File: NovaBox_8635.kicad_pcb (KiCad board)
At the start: 2 copper layers, 53 parts, among them P1 MH, P2 MH, P3 MH, P4 MH, Q1 MMBT3904_l, Q2 IRLML6344, SW1 NEXT, SW2 PREV, SW3 PP, SW4 VOL+, SW5 VOL-, SW6 ON/OFF, U1 CSR8635_MODULE, U2 CSR_DebugSmall, U3 PAM8304, U4 PAM8304

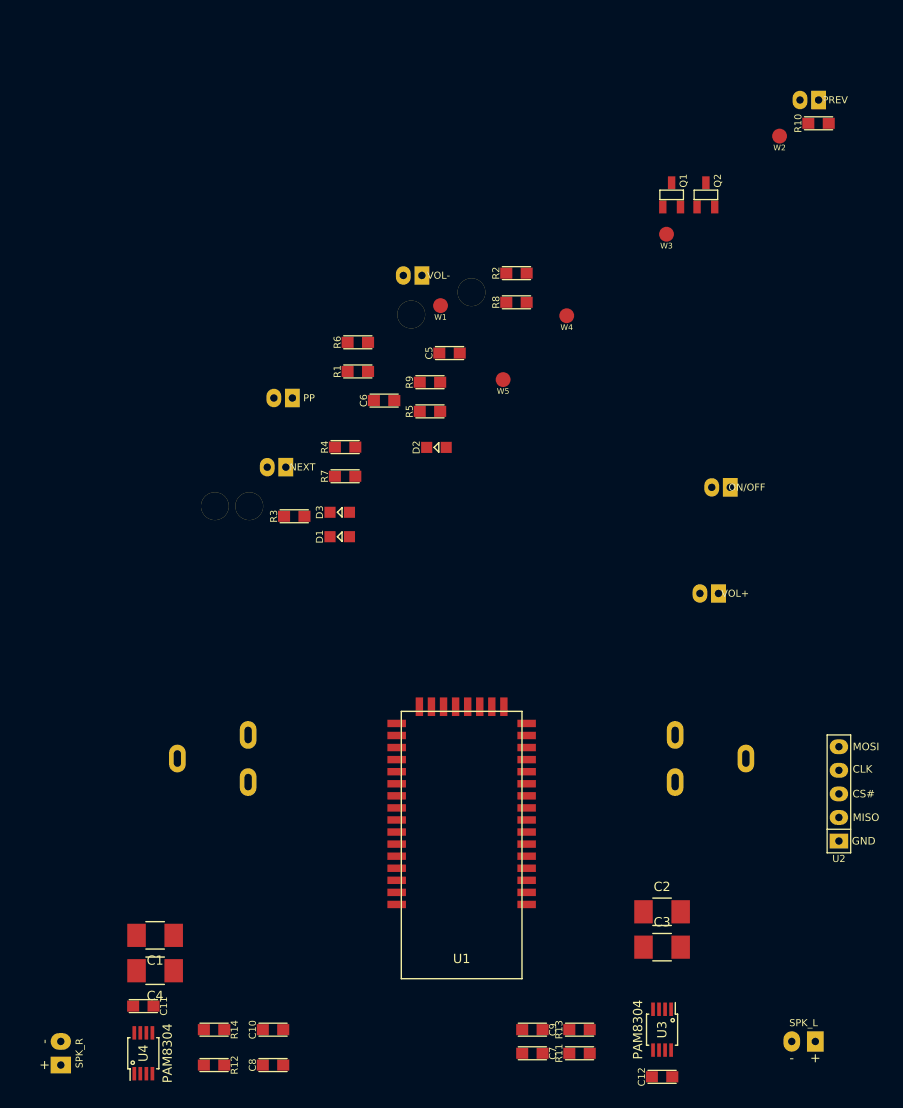
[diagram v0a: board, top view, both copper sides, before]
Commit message: CSR8635 pcb layout
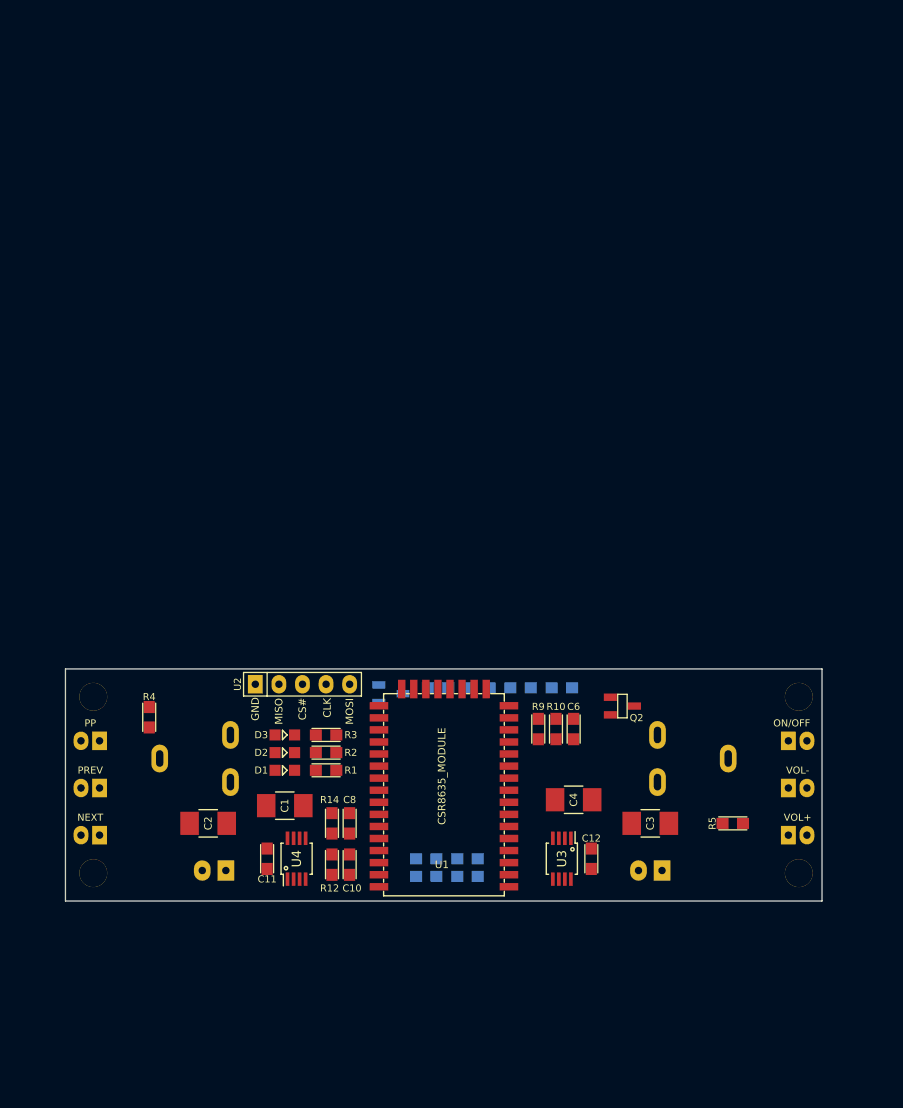
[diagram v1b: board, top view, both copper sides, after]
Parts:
- removed W1: P16, NovaBox:TestPad
- removed W2: P9, NovaBox:TestPad
- removed W3: P0, NovaBox:TestPad
- removed W4: P1, NovaBox:TestPad
- removed W5: P8, NovaBox:TestPad
- C5, C7, C9, Q1, R11, R13, R6, R7, R8, S1, S2: moved to B.Cu
- moved SW2 107.2 mm to (66.7, 123.8)
- moved P4 74.3 mm to (143.0, 133.0)
- moved R10 71.1 mm to (116.8, 117.5), turned to 90 degrees
- moved P2 69.2 mm to (67.0, 133.0)
- moved SW5 69.1 mm to (142.9, 123.8), turned to 180 degrees
- moved Q1 61.7 mm to (99.1, 113.7), turned to 90 degrees
- moved U2 59.0 mm to (89.5, 112.6), turned to 0 degrees
- moved P3 56.1 mm to (143.0, 114.0)
- moved Q2 55.8 mm to (124.0, 115.0), turned to 270 degrees
- moved R2 55.6 mm to (92.1, 120.0), turned to 180 degrees
- moved R5 55.1 mm to (135.9, 127.6)
- moved C2 49.8 mm to (79.4, 127.6), turned to 180 degrees
- moved C4 48.7 mm to (118.7, 125.1)
- moved SW1 44.4 mm to (66.7, 128.9)
- moved R1 43.1 mm to (92.1, 121.9), turned to 180 degrees
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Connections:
- U1 pad 11: Net-(U1-Pad11) -> (no net)
- U1 pad 2: Net-(U1-Pad2) -> (no net)
- U1 pad 3: Net-(U1-Pad3) -> (no net)
- U1 pad 4: Net-(U1-Pad4) -> (no net)
- U1 pad 8: Net-(U1-Pad8) -> (no net)
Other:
- board outline added: 81.5 x 25 mm

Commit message: CSR8635 PCB first draft
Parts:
- Q2, R4, SW1, SW2, SW3, SW4, SW5, SW6: moved to B.Cu
- moved Q2 8.19 mm to (132.1, 113.7), turned to 90 degrees
- moved SW1 5.08 mm to (66.7, 123.8)
- moved SW2 5.08 mm to (66.7, 128.9)
- moved R4 3.97 mm to (70.0, 118.7)
- moved C6 1.27 mm to (120.0, 117.5)
- moved C7 1.27 mm to (104.1, 133.3)
- moved C9 1.27 mm to (104.1, 131.4)
- moved R10 1.27 mm to (118.1, 117.5)
- moved R11 1.27 mm to (108.6, 133.3)
- moved R13 1.27 mm to (108.6, 131.4)
- moved R9 1.27 mm to (116.2, 117.5)
- moved P3 0.50 mm to (142.5, 114.0)
- moved P4 0.50 mm to (142.5, 133.0)
- moved U1 0.38 mm to (104.8, 114.0)
- moved C1 0.28 mm to (87.8, 125.5), turned to 180 degrees
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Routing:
- net +BATT: track 0.00 -> 133.3 mm, vias 0 -> 2
- net 1V8: track 0.00 -> 75.8 mm, vias 0 -> 1
- net NEXT: track 0.00 -> 49.3 mm, vias 0 -> 1
- net PP/CALL: track 0.00 -> 46.8 mm, vias 0 -> 1
- net PREV: track 0.00 -> 46.6 mm, vias 0 -> 1
- net VOL+: track 0.00 -> 36.3 mm
- net VOL-: track 0.00 -> 34.7 mm
- net GND: track 0.00 -> 26.5 mm, vias 0 -> 7
- net LED1: track 0.00 -> 24.4 mm, vias 0 -> 2
- net Net-(Q1-Pad1): track 0.00 -> 20.7 mm
- net Net-(BT1-Pad2): track 0.00 -> 20.3 mm
- net CSR_RST: track 0.00 -> 17.6 mm
- net Net-(U1-Pad23): track 0.00 -> 17.5 mm, vias 0 -> 1
- net Net-(R4-Pad2): track 0.00 -> 15.5 mm
- net Net-(U1-Pad24): track 0.00 -> 14.6 mm
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- added copper zone on B.Cu, net GND
- added copper zone on F.Cu, net GND
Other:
- net class Default: clearance 0.2 -> 0.2032; trace_width 0.25 -> 0.254
- rule trace_clearance: 0.2 -> 0.2032

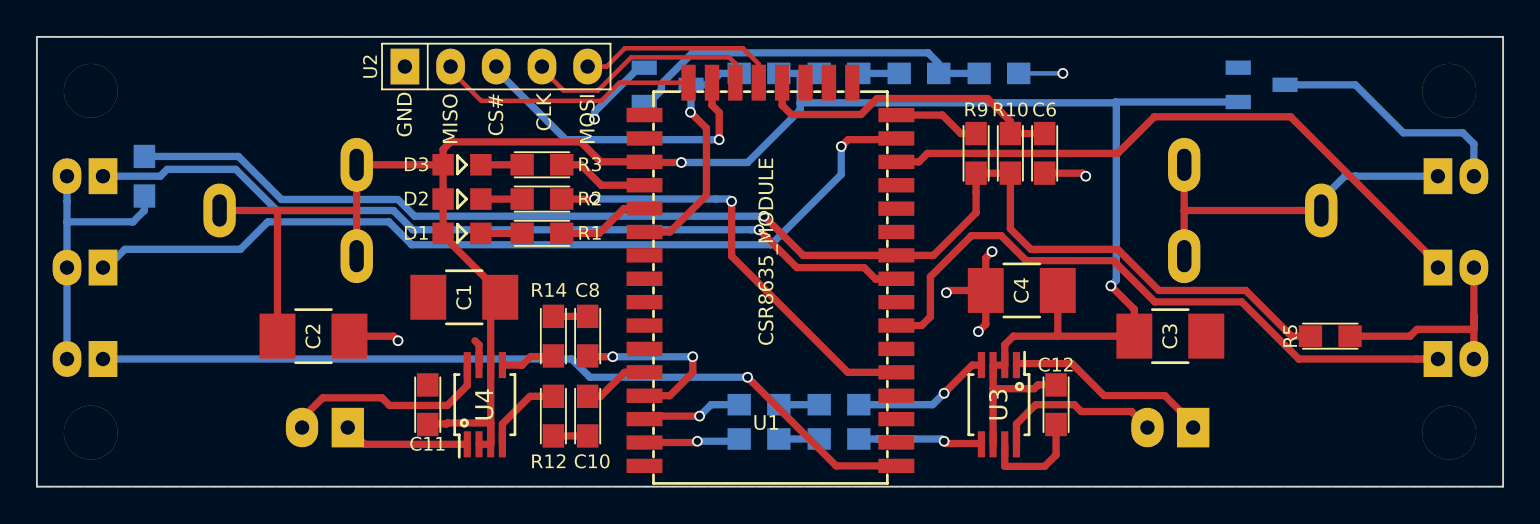
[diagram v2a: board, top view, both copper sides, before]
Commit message: starting to fix 3D models
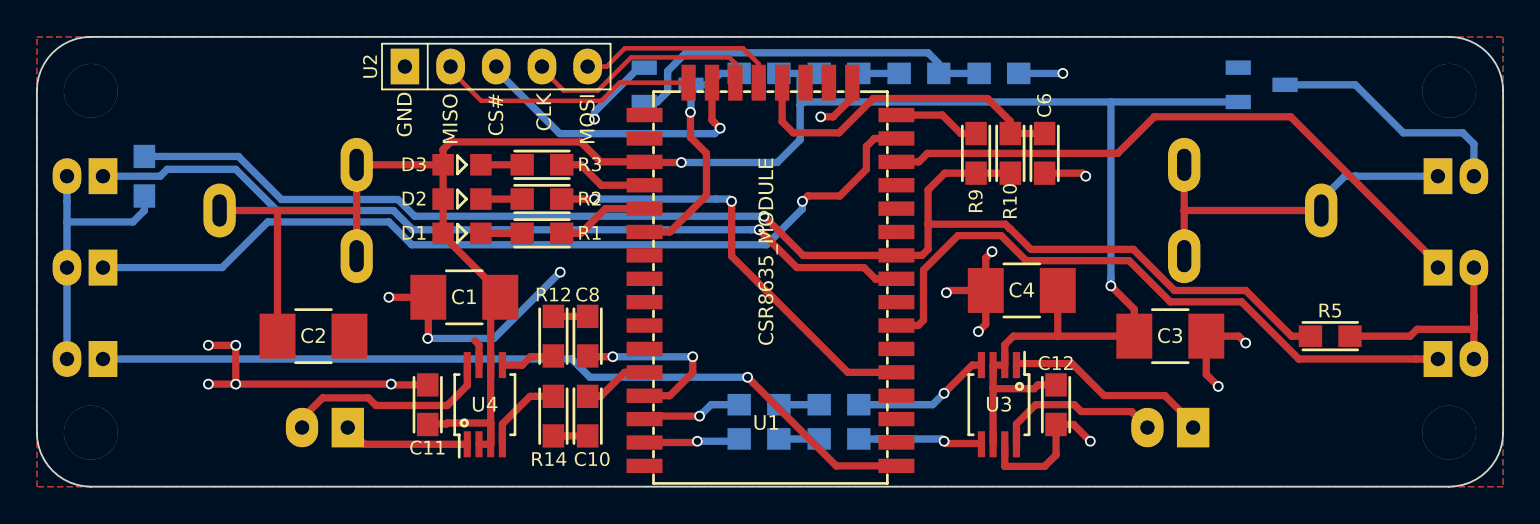
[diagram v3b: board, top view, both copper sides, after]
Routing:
- net GND: track 26.5 -> 63.7 mm, vias 7 -> 18
- net 1V8: track 75.8 -> 78.1 mm
- net CSR_RST: track 17.6 -> 19.0 mm
- net +BATT: track 133.3 -> 134.1 mm
- net Net-(U1-Pad23): track 17.5 -> 17.0 mm
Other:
- outline, holes or cut-outs redrawn

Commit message: CSR8635 PCB second draft
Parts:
- C1, C2, C3, C4: footprint NovaBox:C_1210_HandSoldering -> NovaBox:C_1206
- C10, C11, C12, C5, C6, C7, C8, C9: footprint NovaBox:SMD0805 -> NovaBox:C_0805
- R1, R10, R11, R12, R13, R14, R2, R3, R4, R5, R6, R7, R8, R9: footprint NovaBox:SMD0805 -> NovaBox:R_0805
- moved C2 8.91 mm to (88.3, 127.0), turned to 180 degrees
- moved C3 8.35 mm to (118.7, 126.4)
- moved C4 1.27 mm to (118.7, 123.8), turned to 0 degrees
- moved C1 1.14 mm to (88.3, 124.5)
- moved R12 0.38 mm to (92.3, 127.6)
- moved R14 0.38 mm to (92.3, 132.1)
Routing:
- net GND: track 63.7 -> 47.9 mm, vias 18 -> 16
- net +BATT: track 134.1 -> 123.2 mm
- net 1V8: track 78.1 -> 78.9 mm
- net CSR_RST: track 19.0 -> 18.2 mm
- net Net-(R12-Pad2): track 3.05 -> 2.41 mm
- net Net-(C8-Pad1): track 1.91 -> 2.54 mm
- net Net-(C10-Pad1): track 1.91 -> 2.54 mm
- net Net-(R5-Pad2): track 13.4 -> 13.9 mm
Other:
- board text added: "NovaBox by nodep 2016/11/09"

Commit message: reverted the PWER_E (R3 and R7) to their suggested values
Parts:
- R7: value 10K -> 1K
- R8: value 100K -> 10K
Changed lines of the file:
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@@
     (pad_to_mask_clearance 0)
     (aux_axis_origin 0 0)
-    (visible_elements 7FFFFF7F)
+    (visible_elements 7FFFFFFF)
     (pcbplotparams
       (layerselection 0x010f0_80000001)
@@
       (effects (font (size 0.762 0.762) (thickness 0.127)) (justify mirror))
     )
-    (fp_text value 10K (at 0 0 450) (layer Dwgs.User) hide
+    (fp_text value 1K (at 0 0 450) (layer Dwgs.User) hide
       (effects (font (size 0.127 0.127) (thickness 0.0254)))
     )
@@
       (effects (font (size 0.762 0.762) (thickness 0.127)) (justify mirror))
     )
-    (fp_text value 100K (at 0 0 450) (layer Dwgs.User) hide
-      (effects (font (size 0.127 0.127) (thickness 0.0254)))
-    )
+    (fp_text value 10K (at 0 0 450) (layer Dwgs.User) hide
+      (effects (font (size 0.127 0.127) (thickness 0.0254)))
+    )

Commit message: new schematic, pcb and sym-lib-table
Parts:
- removed D2: BLUE, NovaBox:LED-0805
- removed D3: RED, NovaBox:LED-0805
- added C13: 100pF, NovaBox:C_0805, F.Cu at (134.4, 62.7)
- added C14: 1uF, NovaBox:C_0805, B.Cu at (80.5, 75.7)
- added C15: 1uF, NovaBox:C_0805, B.Cu at (107.2, 75.7)
- added C16: 330pF, NovaBox:C_0805, F.Cu at (127.8, 61.7)
- added C17: 100nF, NovaBox:C_0805, F.Cu at (65.8, 67.6)
- added C18: 100nF, NovaBox:C_0805, F.Cu at (64.8, 71.9)
- added C19: 100nF, NovaBox:C_0805, F.Cu at (80.8, 72.9)
- added C20: 33nF, NovaBox:C_0805, B.Cu at (123.4, 74.4)
- added C21: 47uF, NovaBox:C_1210, F.Cu at (123.5, 68.6)
- added C22: 100nF, NovaBox:C_0805, F.Cu at (82.1, 43.2)
- added D10: Vref 2.5V, NovaBox:SOT-23, F.Cu at (71.4, 76.2)
- added D4: BATT_H, NovaBox:LED_0805, F.Cu at (68.6, 51.6)
- added D5: BATT_M, NovaBox:LED_0805, F.Cu at (68.6, 53.6)
- added D6: BATT_L, NovaBox:LED_0805, F.Cu at (68.6, 55.6)
- added D7: TEMP_H, NovaBox:LED_0805, F.Cu at (73.4, 59.9)
- added D8: MBRS130LT3, NovaBox:SMB_403A, F.Cu at (123.5, 75.0)
- added D9: PWR, NovaBox:LED_0805, F.Cu at (117.6, 64.0)
- added L1: 4.7uH, NovaBox:COIL0608, B.Cu at (128.8, 75.9)
- added P5: USB, NovaBox:USB_MiniB_THT, F.Cu at (111.6, 56.8)
- added Q3: IRLML6401, NovaBox:SOT-23, F.Cu at (75.3, 44.2)
- added Q4: MMBT3904_l, NovaBox:SOT-23, B.Cu at (116.3, 71.2)
- added Q5: MMBT3904_l, NovaBox:SOT-23, F.Cu at (78.7, 44.2)
- added R15: 180K, NovaBox:R_0805, F.Cu at (80.8, 74.9)
- added R16: 510K, NovaBox:R_0805, F.Cu at (80.8, 70.9)
- added R17: 510K, NovaBox:R_0805, F.Cu at (80.3, 67.1)
- added R18: 10K, NovaBox:R_0805, B.Cu at (87.4, 77.2)
- added R19: 10K, NovaBox:R_0805, B.Cu at (100.3, 73.2)
- added R20: 10K, NovaBox:R_0805, B.Cu at (87.4, 73.2)
- added R21: 10K, NovaBox:R_0805, B.Cu at (100.3, 77.2)
- added R22: 33K, NovaBox:R_0805, B.Cu at (119.4, 74.4)
- added R23: 33K, NovaBox:R_0805, B.Cu at (121.4, 74.4)
- added R24: 47K, NovaBox:R_0805, F.Cu at (134.4, 64.8)
- added R25: 316K, NovaBox:R_0805, F.Cu at (127.8, 63.8)
- added R26: 100K, NovaBox:R_0805, F.Cu at (127.8, 59.7)
- added R27: 10K, NovaBox:R_0805, F.Cu at (110.7, 64.8)
- added R29: 10K, NovaBox:R_0805, F.Cu at (66.4, 76.2)
- added R30: 750, NovaBox:R_0805, F.Cu at (68.4, 76.2)
- added RP1: R_Pack04, NovaBox:Resistor_Array_x4_1206, F.Cu at (73.4, 64.8)
- added RP2: R_Pack04, NovaBox:Resistor_Array_x4_1206, F.Cu at (87.9, 61.0)
- added U5: PAM8304, NovaBox:MSOP-8_0.65mmPitch, B.Cu at (104.1, 75.7)
- added U6: LT1308, NovaBox:SOIC-8_3.9x4.9mm_Pitch1.27mm, F.Cu at (130.0, 70.4)
- C1: value 100uF -> 100nF; footprint NovaBox:C_1206 -> NovaBox:C_0805
- C10: value 100nF -> 47uF; footprint NovaBox:C_0805 -> NovaBox:C_1210
- C11: value 1uF -> 47uF; footprint NovaBox:C_0805 -> NovaBox:C_1210; moved to B.Cu
- C12: value 1uF -> 47uF; footprint NovaBox:C_0805 -> NovaBox:C_1210
- C2, C3: value 100uF -> 1uF; footprint NovaBox:C_1206 -> NovaBox:C_0805
- C4: value 100uF -> 1uF; footprint NovaBox:C_1206 -> NovaBox:C_0805; moved to B.Cu
- C6: value 100nF -> 1uF; moved to B.Cu
- C7: value 100nF -> 1uF
- C8: value 100nF -> 47uF; footprint NovaBox:C_0805 -> NovaBox:C_1210; moved to B.Cu
- C9: value 100nF -> 47uF; footprint NovaBox:C_0805 -> NovaBox:C_1210; moved to F.Cu
- D1: value GREEN -> LED_RABG_l; footprint NovaBox:LED-0805 -> NovaBox:PLCC4
- Q1, Q2: footprint NovaBox:SOT23 -> NovaBox:SOT-23; moved to F.Cu
- R1, R2, R3: value 1K -> 33K
- R10: value 10K -> 180K
- R11: value 1K -> 270K; moved to F.Cu
- R12, R14: value 1K -> 510K
- R13: value 1K -> 220K; moved to F.Cu
- R4, R6, R7, R8: moved to F.Cu
- R5, R9: value 10K -> 1K
- SW1: value NEXT -> PIO18
- SW2: value PREV -> PIO21
- SW3: value PP -> PIO8
- SW4: value VOL+ -> PIO0
- SW5: value VOL- -> PIO1
- SW6: footprint NovaBox:Switch_2mm -> NovaBox:Switch_2.5mm
- U1: value CSR8635_MODULE -> MCP6004; footprint NovaBox:CSR8635_MODULE -> NovaBox:TSSOP-14_4.4x5mm_Pitch0.65mm
- U2: value CSR_DebugSmall -> CSR8635_MODULE; footprint NovaBox:CSR_DebugSmall -> NovaBox:CSR8635_MODULE
- U3: value PAM8304 -> CSR_DebugSmall; footprint NovaBox:MSOP-8_0.65mmPitch -> NovaBox:CSR_DebugSmall
- U4: moved to B.Cu
- moved P4 113.5 mm to (62.0, 53.0)
- moved P2 107.0 mm to (138.0, 53.0)
- moved C3 86.2 mm to (90.5, 44.9)
- moved U3 82.8 mm to (96.0, 51.4), turned to 0 degrees
- moved R11 81.9 mm to (65.8, 63.5), turned to 180 degrees
- moved S1 74.5 mm to (76.4, 78.0), turned to 180 degrees
- moved R3 73.9 mm to (129.2, 54.2), turned to 90 degrees
- moved C2 73.0 mm to (85.1, 54.1)
- moved C10 72.9 mm to (134.8, 71.3)
- moved R13 71.6 mm to (68.8, 71.9), turned to 270 degrees
- moved R8 71.0 mm to (81.0, 52.1), turned to 0 degrees
- moved SW2 70.1 mm to (61.0, 59.0), turned to 90 degrees
- moved R5 68.2 mm to (117.6, 62.0), turned to 180 degrees
- moved R12 67.5 mm to (65.8, 65.5), turned to 180 degrees
- moved R7 67.1 mm to (85.1, 52.1), turned to 0 degrees
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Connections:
- C1 pad 1: +BATT -> CSR_RST
- C10 pad 1: Net-(C10-Pad1) -> +BATT
- C10 pad 2: Net-(C10-Pad2) -> GND
- C11 pad 1: +BATT -> +5V
- C12 pad 1: +BATT -> +5V
- C2 pad 2: GND -> Net-(C2-Pad2)
- C3 pad 1: +BATT -> GND
- C3 pad 2: GND -> Net-(C3-Pad2)
- C4 pad 1: +BATT -> Net-(C4-Pad1)
- C4 pad 2: GND -> Net-(C4-Pad2)
- C5 pad 1: +BATT -> Net-(C5-Pad1)
- C6 pad 1: CSR_RST -> Net-(C6-Pad1)
- C6 pad 2: GND -> Net-(C6-Pad2)
- C8 pad 1: Net-(C8-Pad1) -> +5V
- C8 pad 2: Net-(C8-Pad2) -> GND
- C9 pad 1: Net-(C9-Pad1) -> +5V
- C9 pad 2: Net-(C9-Pad2) -> GND
- R1 pad 1: LED2 -> +BATT
- R1 pad 2: Net-(D1-Pad1) -> Net-(Q3-Pad1)
- R10 pad 1: 1V8 -> Net-(C22-Pad1)
- R10 pad 2: CSR_RST -> +BATT
- R11 pad 1: Net-(C7-Pad1) -> Net-(C17-Pad1)
- R11 pad 2: Net-(R11-Pad2) -> +BATT
- R12 pad 1: Net-(C8-Pad1) -> Net-(C17-Pad1)
- R12 pad 2: Net-(R12-Pad2) -> GND
- R13 pad 1: Net-(C9-Pad1) -> Net-(C18-Pad1)
- R13 pad 2: Net-(R13-Pad2) -> +BATT
- R14 pad 1: Net-(C10-Pad1) -> Net-(C18-Pad1)
- R14 pad 2: Net-(R14-Pad2) -> GND
- R2 pad 1: LED1 -> Net-(C3-Pad2)
- R2 pad 2: Net-(D2-Pad1) -> 1V8
- R3 pad 1: LED0 -> VR_SHDN
- R3 pad 2: Net-(D3-Pad1) -> GND
- R4 pad 1: 1V8 -> PWER_E
- R4 pad 2: Net-(R4-Pad2) -> +BATT
- R5 pad 1: 1V8 -> GND
- R5 pad 2: Net-(R5-Pad2) -> Net-(D9-Pad1)
- R6 pad 1: PWER_E -> 1V8
- R6 pad 2: +BATT -> CSR_RST
- R7 pad 2: Net-(C5-Pad2) -> Net-(C2-Pad2)
- R9 pad 2: SPI_PCM -> Net-(R9-Pad2)
- SW1 pad 1: NEXT -> PIO18
- SW1 pad 2: Net-(R4-Pad2) -> Net-(R9-Pad2)
- SW2 pad 1: PREV -> PIO21
- SW2 pad 2: Net-(R4-Pad2) -> Net-(R9-Pad2)
- SW3 pad 1: PP/CALL -> PIO8
- SW3 pad 2: Net-(R4-Pad2) -> Net-(R9-Pad2)
- SW4 pad 1: VOL+ -> PIO0
- SW4 pad 2: Net-(R5-Pad2) -> Net-(R9-Pad2)
- SW5 pad 1: VOL- -> PIO1
- SW5 pad 2: Net-(R5-Pad2) -> Net-(R9-Pad2)
- U1 pad 1: PREV -> Net-(RP1-Pad1)
- U1 pad 10: 1V8 -> Net-(C19-Pad1)
- U1 pad 11: (no net) -> GND
- U1 pad 12: (no net) -> Net-(C22-Pad1)
- U1 pad 13: (no net) -> 2V5
- U1 pad 14: VOL- -> Net-(RP1-Pad4)
- U1 pad 2: (no net) -> 2V5
- U1 pad 3: (no net) -> Net-(C17-Pad1)
- U1 pad 5: LED1 -> Net-(C18-Pad1)
- U1 pad 6: (no net) -> 2V5
- U1 pad 7: VOL+ -> Net-(RP1-Pad2)
- U1 pad 8: (no net) -> Net-(RP1-Pad3)
- U1 pad 9: PP/CALL -> 2V5
- U2 pad 1: Net-(U1-Pad21) -> (no net)
- U2 pad 2: Net-(U1-Pad22) -> PIO8
- U2 pad 3: Net-(U1-Pad23) -> PIO1
- U2 pad 4: Net-(U1-Pad24) -> PIO0
- U2 pad 5: GND -> LED1
- U3 pad 1: Net-(S1-Pad1) -> Net-(U2-Pad21)
- U3 pad 2: +BATT -> Net-(U2-Pad22)
- U3 pad 3: +BATT -> Net-(U2-Pad23)
- U3 pad 4: Net-(R13-Pad2) -> Net-(U2-Pad24)
- U3 pad 5: Net-(R11-Pad2) -> GND
- U4 pad 1: Net-(S2-Pad1) -> Net-(S1-Pad1)
- U4 pad 2: +BATT -> +5V
- U4 pad 3: +BATT -> +5V
- U4 pad 4: Net-(R14-Pad2) -> BTLN
- U4 pad 5: Net-(R12-Pad2) -> BTLP
- U4 pad 6: +BATT -> +5V
- U4 pad 8: Net-(S2-Pad2) -> Net-(S1-Pad2)
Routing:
- net Net-(R9-Pad2): track 0.00 -> 134.6 mm, vias 0 -> 2
- net +5V: track 0.00 -> 129.2 mm, vias 0 -> 6
- net 1V8: track 78.9 -> 12.3 mm, vias 1 -> 0
- net Net-(BT1-Pad2): track 20.3 -> 81.1 mm, vias 0 -> 1
- net PIO18: track 0.00 -> 59.5 mm, vias 0 -> 1
- net PIO21: track 0.00 -> 54.4 mm, vias 0 -> 1
- net PIO8: track 0.00 -> 50.7 mm, vias 0 -> 1
- net NEXT: track 49.1 -> 0.00 mm, vias 1 -> 0
- net PP/CALL: track 46.8 -> 0.00 mm, vias 1 -> 0
- net PREV: track 46.6 -> 0.00 mm, vias 1 -> 0
- net 2V5: track 0.00 -> 45.1 mm
- net PIO0: track 0.00 -> 43.0 mm
- net PIO1: track 0.00 -> 37.5 mm
- net VOL+: track 37.1 -> 0.00 mm
- net VOL-: track 34.7 -> 0.00 mm
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- added copper zone on F.Cu, net +5V
- added copper zone on F.Cu, net +BATT
- added copper zone on F.Cu, net /SW
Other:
- board size 81.5 x 25 mm -> 82 x 30 mm
- net class Default: trace_width 0.254 -> 0.2032; via_dia 0.6 -> 0.8
- board text added: "2017.feb.15"
- board text added: "8Ω"
- board text added: "BTRY"
- board text added: "NovaBox"
- board text added: "by čika c"
- board text added: "https://github.com/nodep/NovaBox"
- board text removed: "NovaBox by nodep 2016/11/09"

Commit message: some cleanup
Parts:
- D1: value LED_RABG_l -> LED_RABG
- Q1, Q4, Q5: value MMBT3904_l -> MMBT3904
- moved C3 2.48 mm to (89.2, 47.0)
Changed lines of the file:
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@@
       (effects (font (size 0.75 0.75) (thickness 0.15)))
     )
-    (fp_text value MMBT3904_l (at 0 0 270) (layer F.Fab)
+    (fp_text value MMBT3904 (at 0 0 270) (layer F.Fab)
       (effects (font (size 0.127 0.127) (thickness 0.03175)))
     )
@@
       (effects (font (size 0.762 0.762) (thickness 0.127)))
     )
-    (fp_text value LED_RABG_l (at 0 0 270) (layer F.Fab) hide
+    (fp_text value LED_RABG (at 0 0 270) (layer F.Fab) hide
       (effects (font (size 0.127 0.127) (thickness 0.0127)))
     )
@@
       (effects (font (size 0.75 0.75) (thickness 0.15)) (justify mirror))
     )
-    (fp_text value MMBT3904_l (at 0 0 90) (layer B.Fab)
+    (fp_text value MMBT3904 (at 0 0 90) (layer B.Fab)
       (effects (font (size 0.127 0.127) (thickness 0.03175)) (justify mirror))
     )
@@
   )
   (module NovaBox:C_0805 (layer F.Cu)
-    (at 90.4875 44.8945)
+    (at 89.17 46.99)
     (descr "Capacitor SMD 0805, reflow soldering, AVX (see smccp.pdf)")
     (tags "capacitor 0805")
@@
       (effects (font (size 0.75 0.75) (thickness 0.15)))
     )
-    (fp_text value MMBT3904_l (at 0 0) (layer F.Fab)
+    (fp_text value MMBT3904 (at 0 0) (layer F.Fab)
       (effects (font (size 0.127 0.127) (thickness 0.03175)))
     )
